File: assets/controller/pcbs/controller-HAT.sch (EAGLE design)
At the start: 12 parts

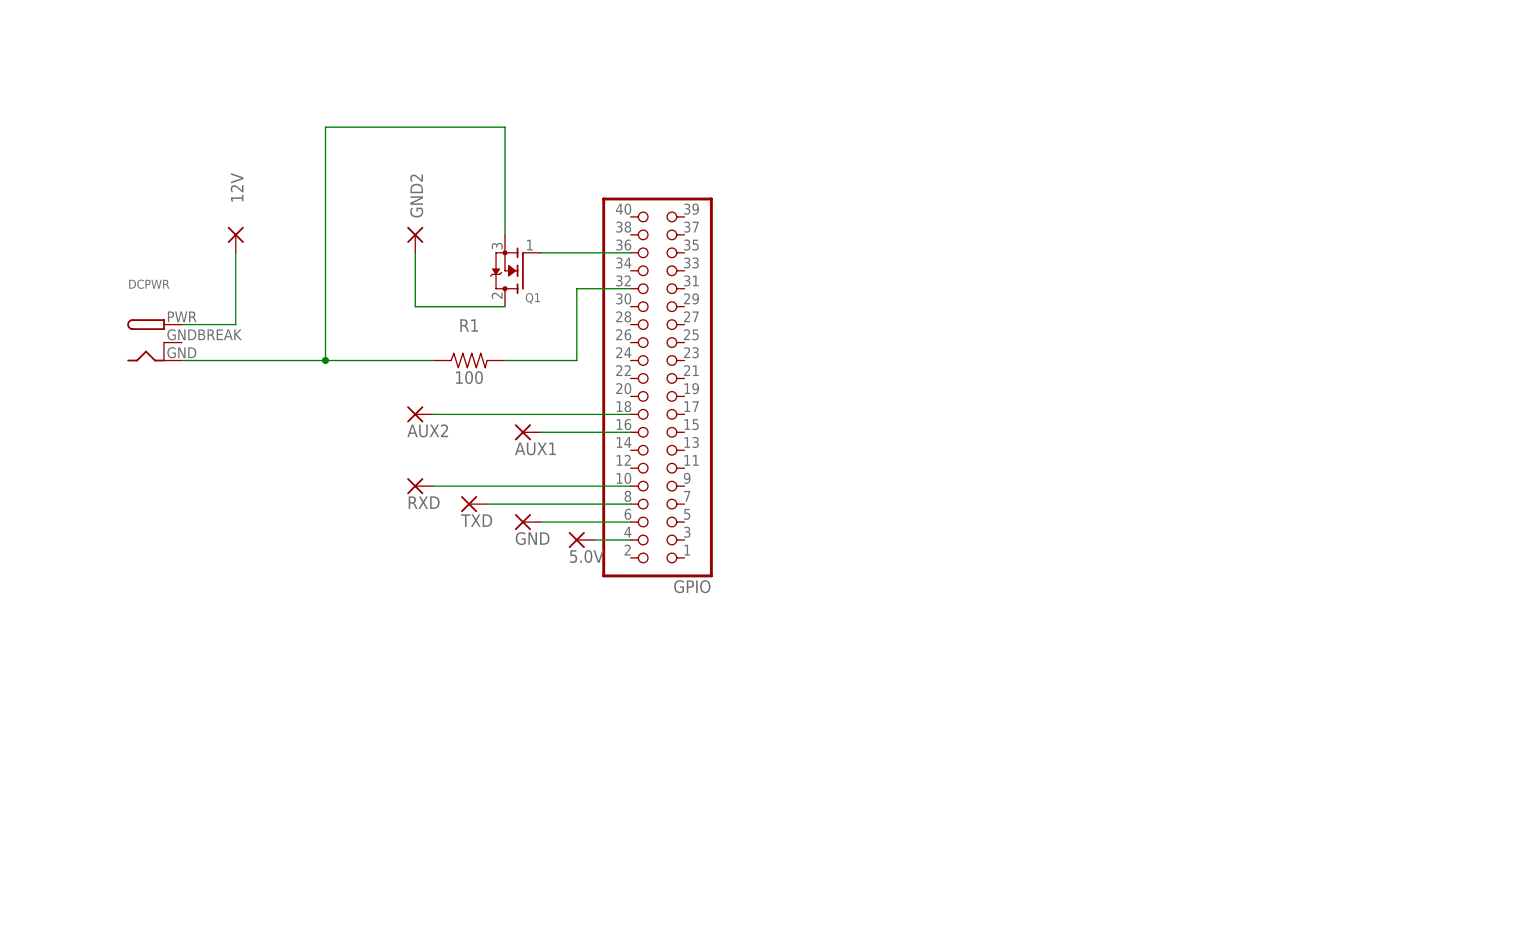
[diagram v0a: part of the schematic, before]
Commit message: Updated the controller hat.
This commit updates the controller hat to include a voltage regulator. This will
allow a single, 12v power source to power both the strike and the raspberry pi
through the 5v pin.
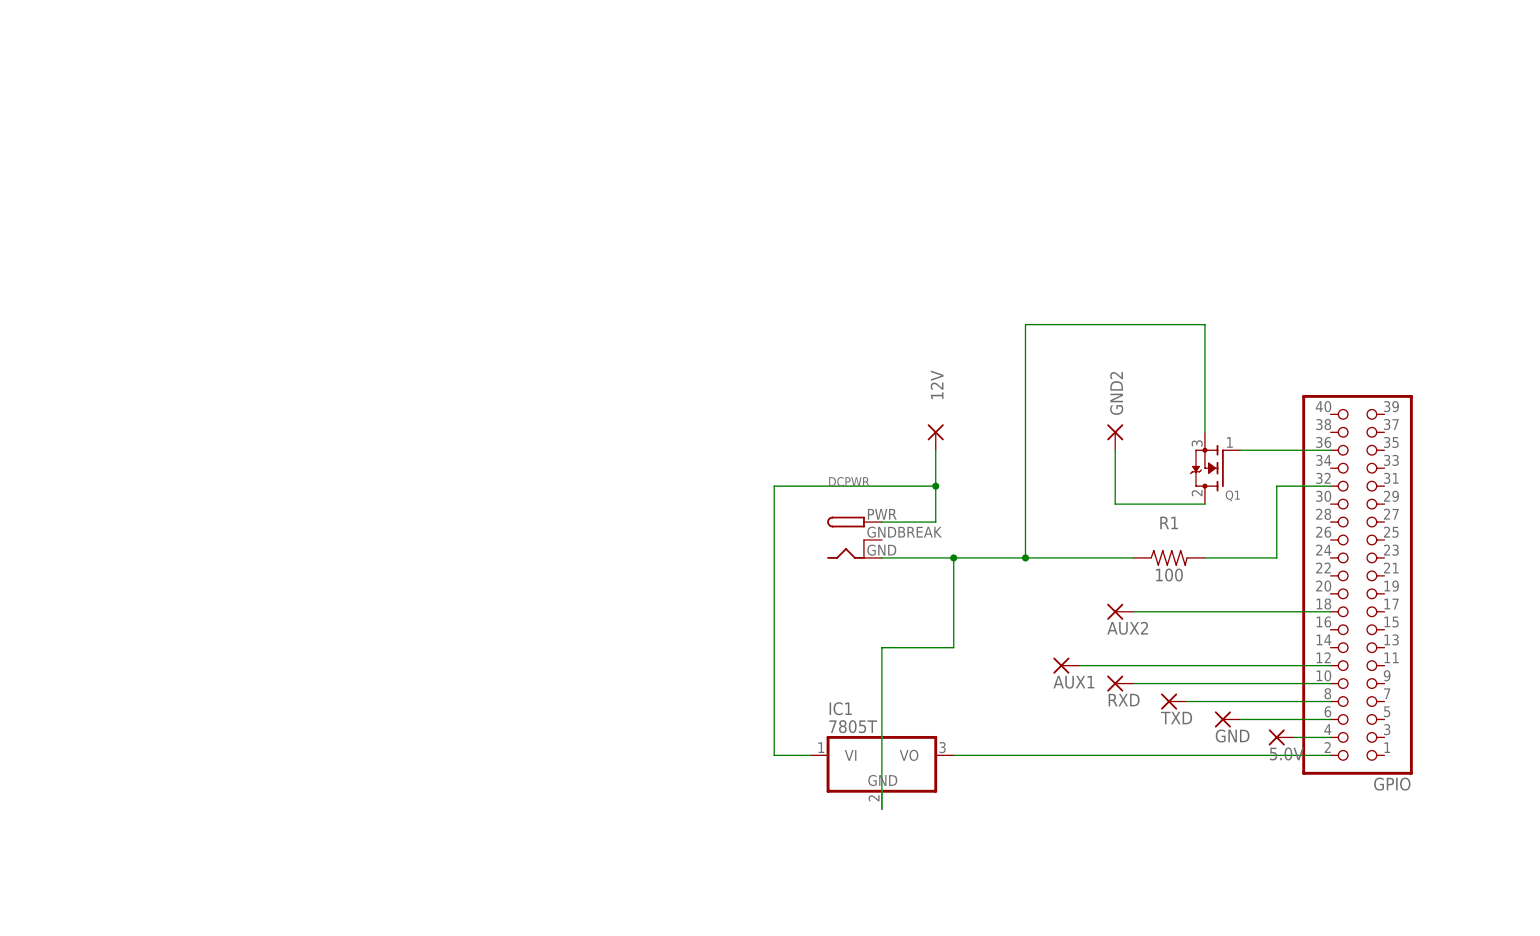
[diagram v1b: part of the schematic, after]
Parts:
- added IC1: 7805T, adafruit:7805T
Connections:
- new net N$12: GPIO.2, IC1.VO
- net N$10: now also GPIO.12; no longer GPIO.16
- net N$2: now also IC1.VI
- net N$4: now also IC1.GND
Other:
- moved on the sheet: 12V, 5.0V, AUX1, AUX2, DCPWR, GND, GND2, GPIO, Q1, R1, RXD, TXD
